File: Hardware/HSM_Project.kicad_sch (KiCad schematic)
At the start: 0 parts

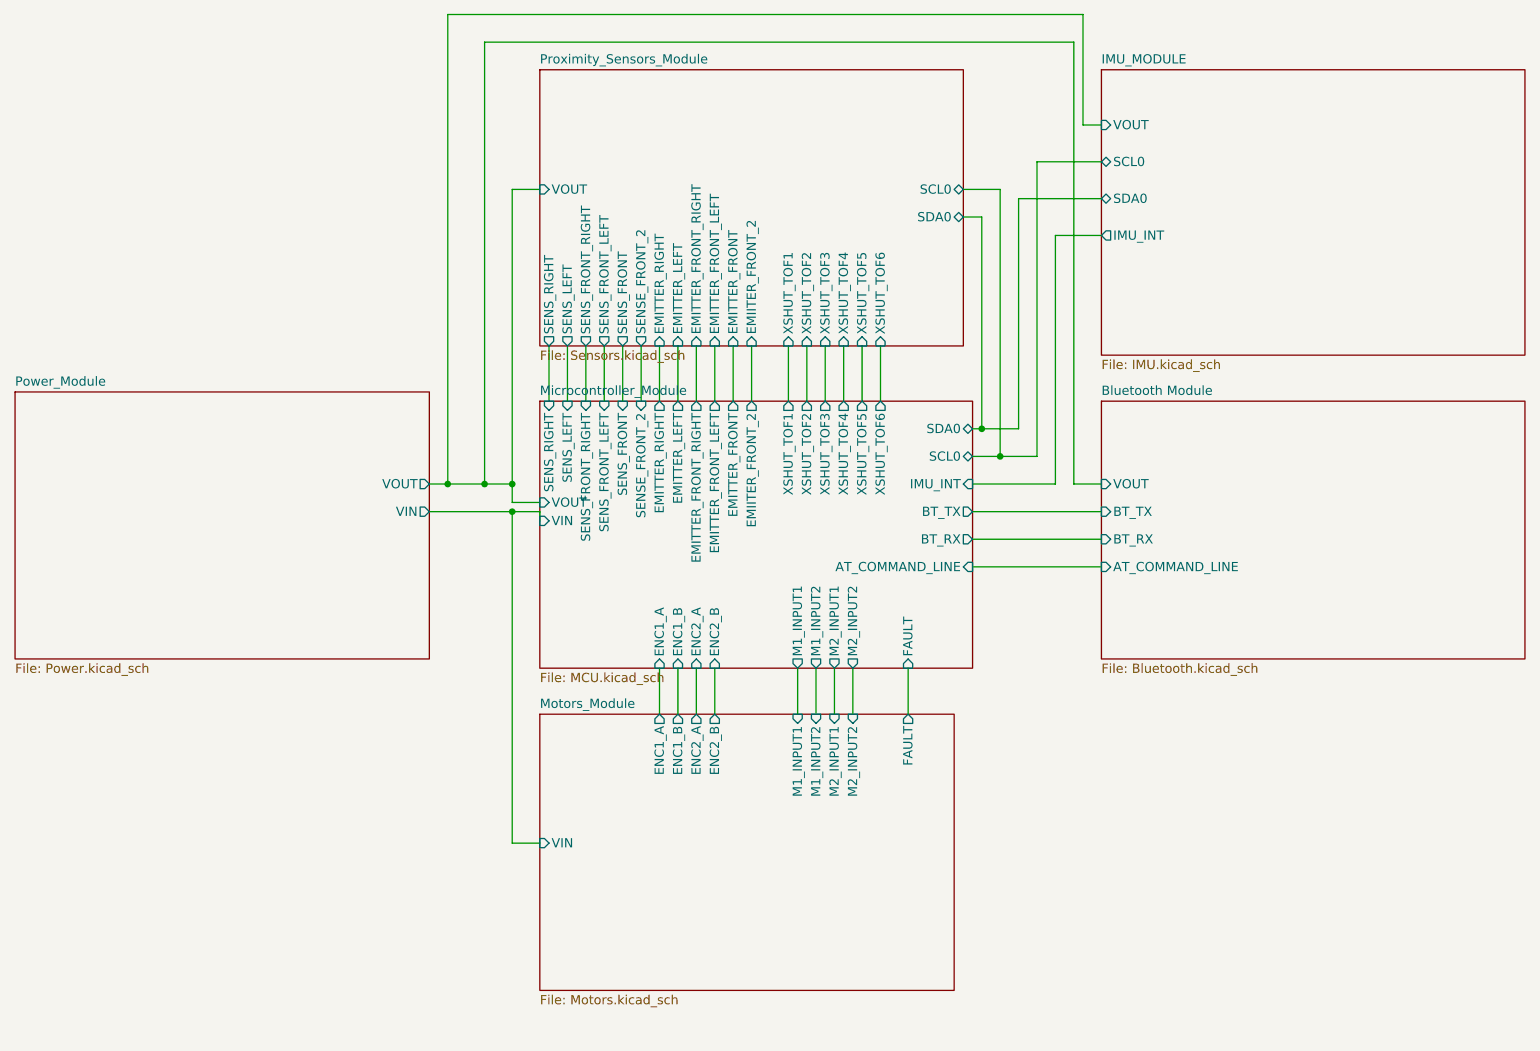
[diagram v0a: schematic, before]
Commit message: Schematic updated with buck and motor driver breakout boards
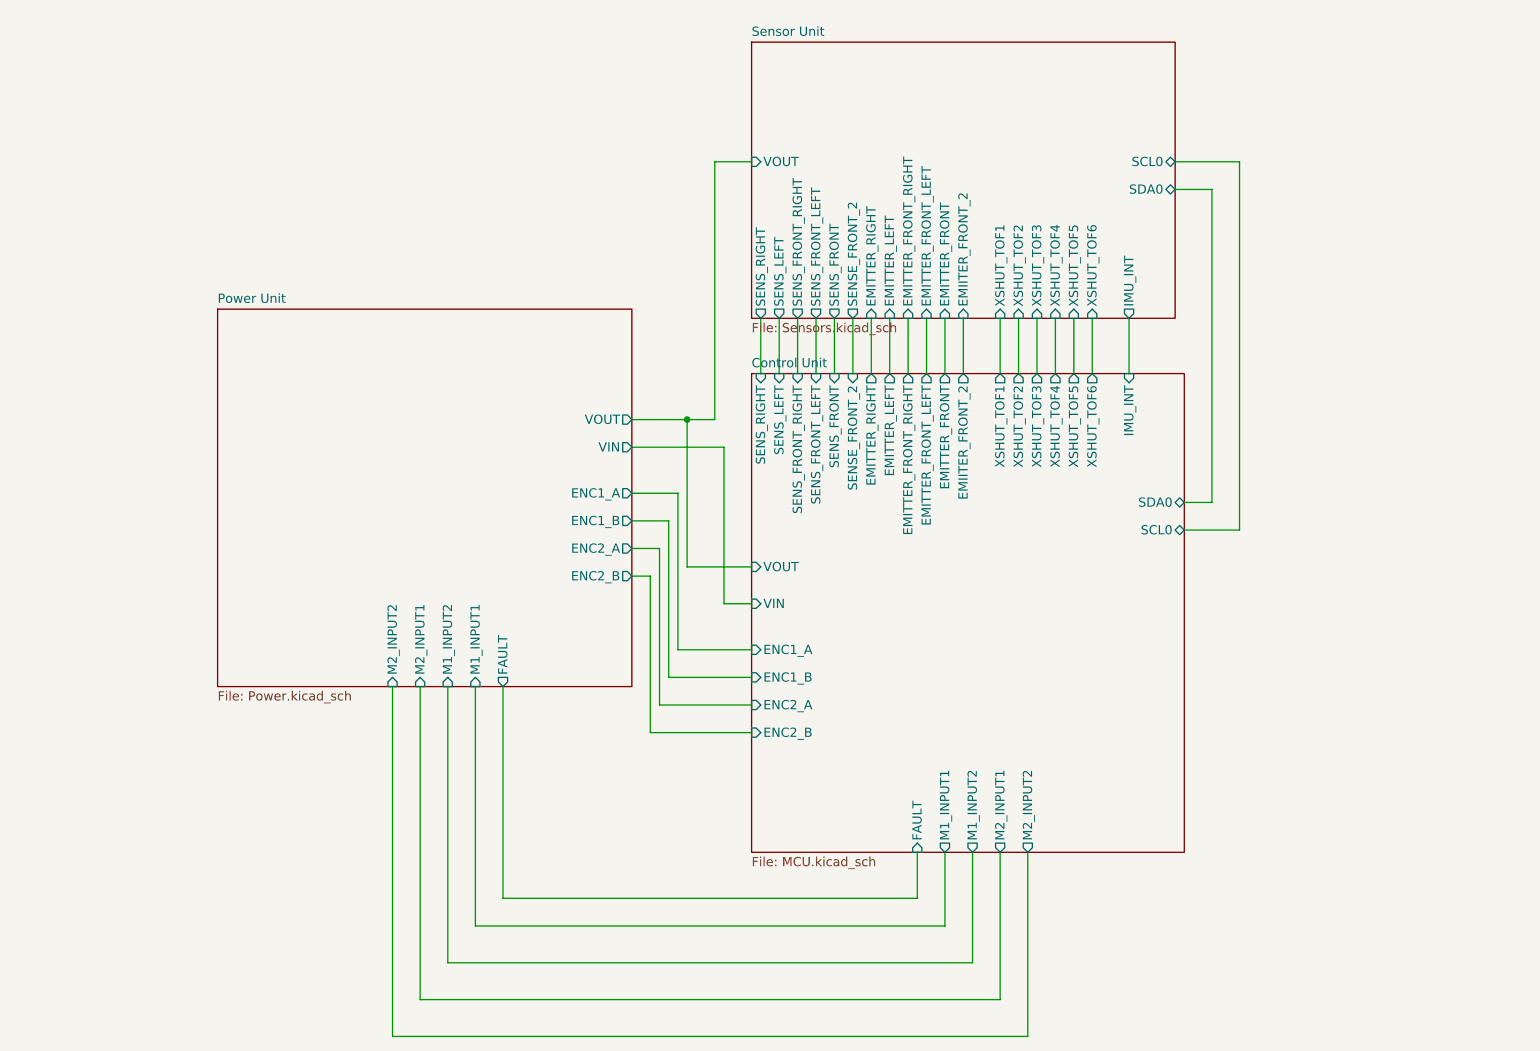
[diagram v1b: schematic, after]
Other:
- sheet Microcontroller_Module renamed Control Unit
- sheet Power_Module renamed Power Unit
- sheet Proximity_Sensors_Module renamed Sensor Unit
- removed sheet Bluetooth Module
- removed sheet IMU_MODULE
- removed sheet Motors_Module
- sheet Control Unit ports: added none; removed AT_COMMAND_LINE, BT_RX, BT_TX
- sheet Power Unit ports: added ENC1_A, ENC1_B, ENC2_A, ENC2_B, FAULT, M1_INPUT1, M1_INPUT2, M2_INPUT1, M2_INPUT2; removed none
- sheet Sensor Unit ports: added IMU_INT; removed none

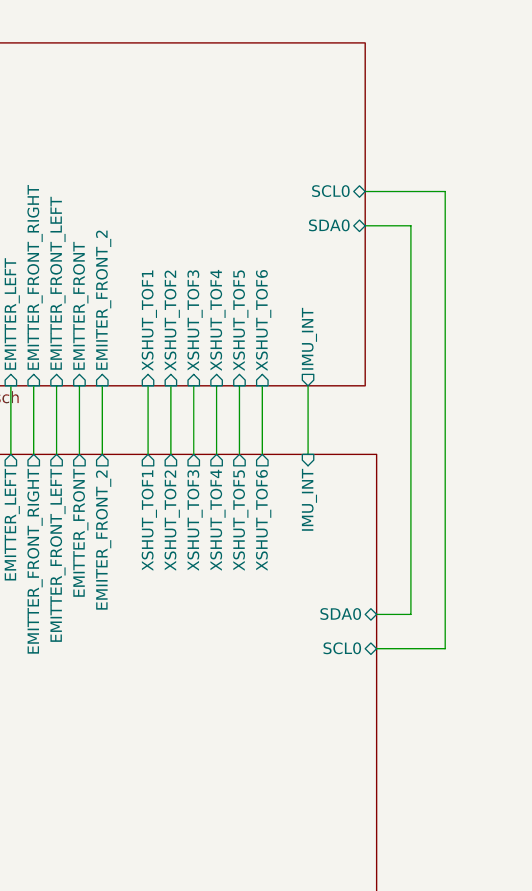
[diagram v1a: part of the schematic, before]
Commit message: 1)PCB tracing continued, power traces need to verified,signal traces almost done except xshut, need to verify drv8833 dimesnions, should resolve teensy 4.1 error, switches footprint need to be changed. 2) changed schematic for optimum tracing in pcb editor,removed oled and added one more extra i2c bus to prevent i2c locking
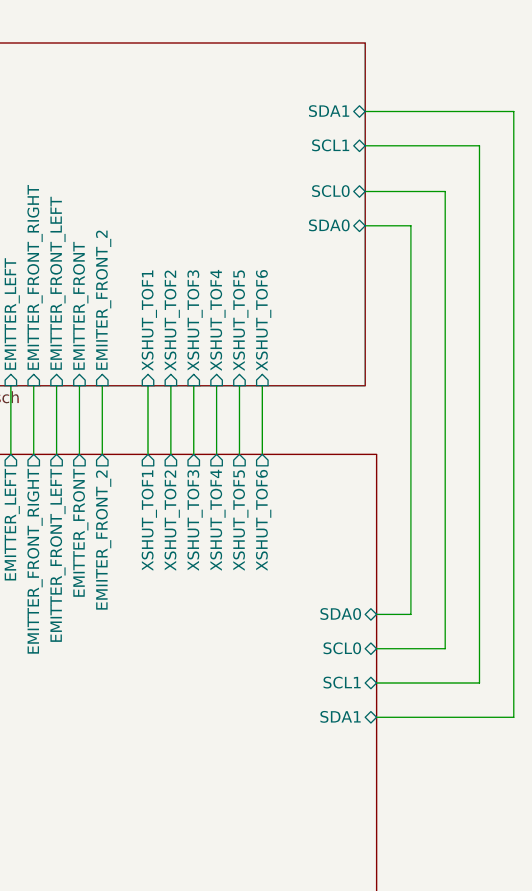
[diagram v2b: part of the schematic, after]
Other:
- sheet Control Unit ports: added SCL1, SDA1; removed IMU_INT
- sheet Sensor Unit ports: added SCL1, SDA1; removed IMU_INT
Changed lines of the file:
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@@
 	(wire
 		(pts
-			(xy 198.12 62.23) (xy 198.12 69.85)
+			(xy 220.98 99.06) (xy 205.74 99.06)
 		)
 		(stroke
@@
 	(wire
 		(pts
+			(xy 204.47 31.75) (xy 220.98 31.75)
+		)
+		(stroke
+			(width 0)
+			(type default)
+		)
+	)
+	(wire
+		(pts
 			(xy 129.54 76.2) (xy 137.16 76.2)
 		)
@@
 	(wire
 		(pts
+			(xy 217.17 95.25) (xy 217.17 35.56)
+		)
+		(stroke
+			(width 0)
+			(type default)
+		)
+	)
+	(wire
+		(pts
+			(xy 217.17 35.56) (xy 204.47 35.56)
+		)
+		(stroke
+			(width 0)
+			(type default)
+		)
+	)
+	(wire
+		(pts
 			(xy 137.16 76.2) (xy 137.16 96.52)
 		)
@@
 	(wire
 		(pts
+			(xy 220.98 31.75) (xy 220.98 99.06)
+		)
+		(stroke
+			(width 0)
+			(type default)
+		)
+	)
+	(wire
+		(pts
 			(xy 180.34 156.21) (xy 180.34 135.89)
 		)
@@
 		(pts
 			(xy 111.76 142.24) (xy 168.91 142.24)
+		)
+		(stroke
+			(width 0)
+			(type default)
+		)
+	)
+	(wire
+		(pts
+			(xy 205.74 95.25) (xy 217.17 95.25)
 		)
 		(stroke
@@
 			)
 		)
-		(pin "IMU_INT" input
-			(at 198.12 69.85 90)
-			(effects
-				(font
-					(size 1.27 1.27)
-				)
-				(justify right)
-			)
-		)
 		(pin "XSHUT_TOF5" output
 			(at 190.5 69.85 90)
@@
 		(pin "XSHUT_TOF6" output
 			(at 193.04 69.85 90)
+			(effects
+				(font
+					(size 1.27 1.27)
+				)
+				(justify right)
+			)
+		)
+		(pin "SCL1" bidirectional
+			(at 205.74 95.25 0)
+			(effects
+				(font
+					(size 1.27 1.27)
+				)
+				(justify right)
+			)
+		)
+		(pin "SDA1" bidirectional
+			(at 205.74 99.06 0)
 			(effects
 				(font
@@
 			)
 		)
-		(pin "IMU_INT" output
-			(at 198.12 62.23 270)
-			(effects
-				(font
-					(size 1.27 1.27)
-				)
-				(justify left)
-			)
-		)
+		(pin "SDA1" bidirectional
+			(at 204.47 31.75 0)
+			(effects
+				(font
+					(size 1.27 1.27)
+				)
+				(justify right)
+			)
+		)
+		(pin "SCL1" bidirectional
+			(at 204.47 35.56 0)
+			(effects
+				(font
+					(size 1.27 1.27)
+				)
+				(justify right)
+			)
+		)

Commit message: Final updated pcb and schematic before dfm check
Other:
- sheet Control Unit ports: added INT_GPIO, RST_GPIO; removed VIN, VOUT
- sheet Power Unit ports: added none; removed VIN, VOUT
- sheet Sensor Unit ports: added INT_GPIO, RST_GPIO; removed VOUT

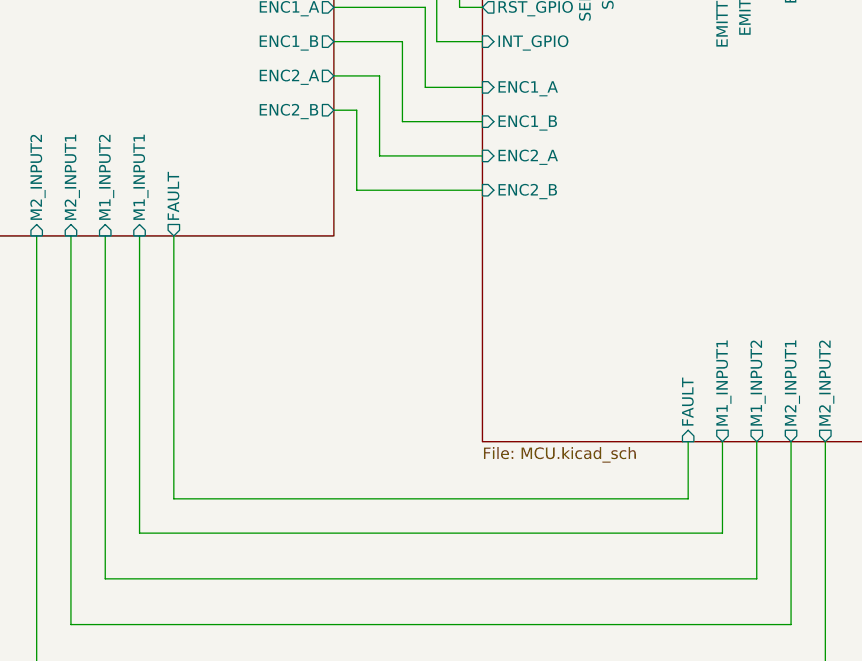
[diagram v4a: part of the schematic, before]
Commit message: updated the dimensiosn of tb6612,shifted placements based on dfm check, other changes
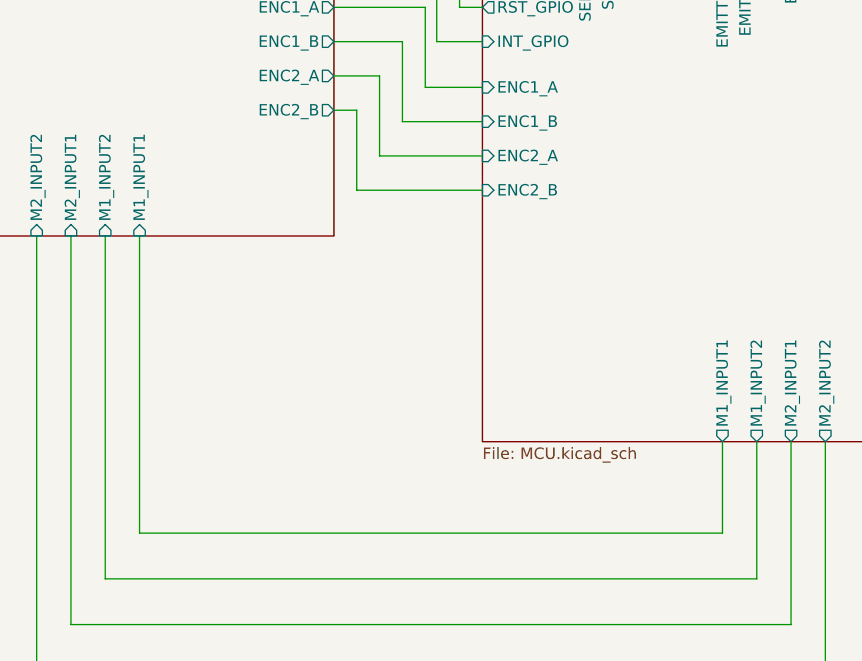
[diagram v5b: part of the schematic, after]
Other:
- sheet Control Unit ports: added none; removed FAULT
- sheet Power Unit ports: added none; removed FAULT
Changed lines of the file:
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@@
-	(wire
-		(pts
-			(xy 111.76 113.03) (xy 111.76 142.24)
-		)
-		(stroke
-			(width 0)
-			(type default)
-		)
-	)
 	(wire
 		(pts
@@
 	(wire
 		(pts
-			(xy 111.76 142.24) (xy 168.91 142.24)
-		)
-		(stroke
-			(width 0)
-			(type default)
-		)
-	)
-	(wire
-		(pts
 			(xy 205.74 95.25) (xy 217.17 95.25)
 		)
@@
 		(pts
 			(xy 146.05 87.63) (xy 143.51 87.63)
-		)
-		(stroke
-			(width 0)
-			(type default)
-		)
-	)
-	(wire
-		(pts
-			(xy 168.91 142.24) (xy 168.91 135.89)
 		)
 		(stroke
@@
 				)
 				(justify right)
-			)
-		)
-		(pin "FAULT" input
-			(at 168.91 135.89 270)
-			(effects
-				(font
-					(size 1.27 1.27)
-				)
-				(justify left)
 			)
 		)
@@
 			(effects
 				(font
-					(size 1.27 1.27)
-				)
-				(justify left)
-			)
-		)
-		(pin "FAULT" output
-			(at 111.76 113.03 270)
-			(effects
-				(font
